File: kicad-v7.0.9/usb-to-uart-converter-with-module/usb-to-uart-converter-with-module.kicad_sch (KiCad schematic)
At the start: 10 parts, among them P1 1x10_pin_header, P2 1x10_pin_header, P3 MLW06A, Q1 MMBT2222, Q2 MMBT2222

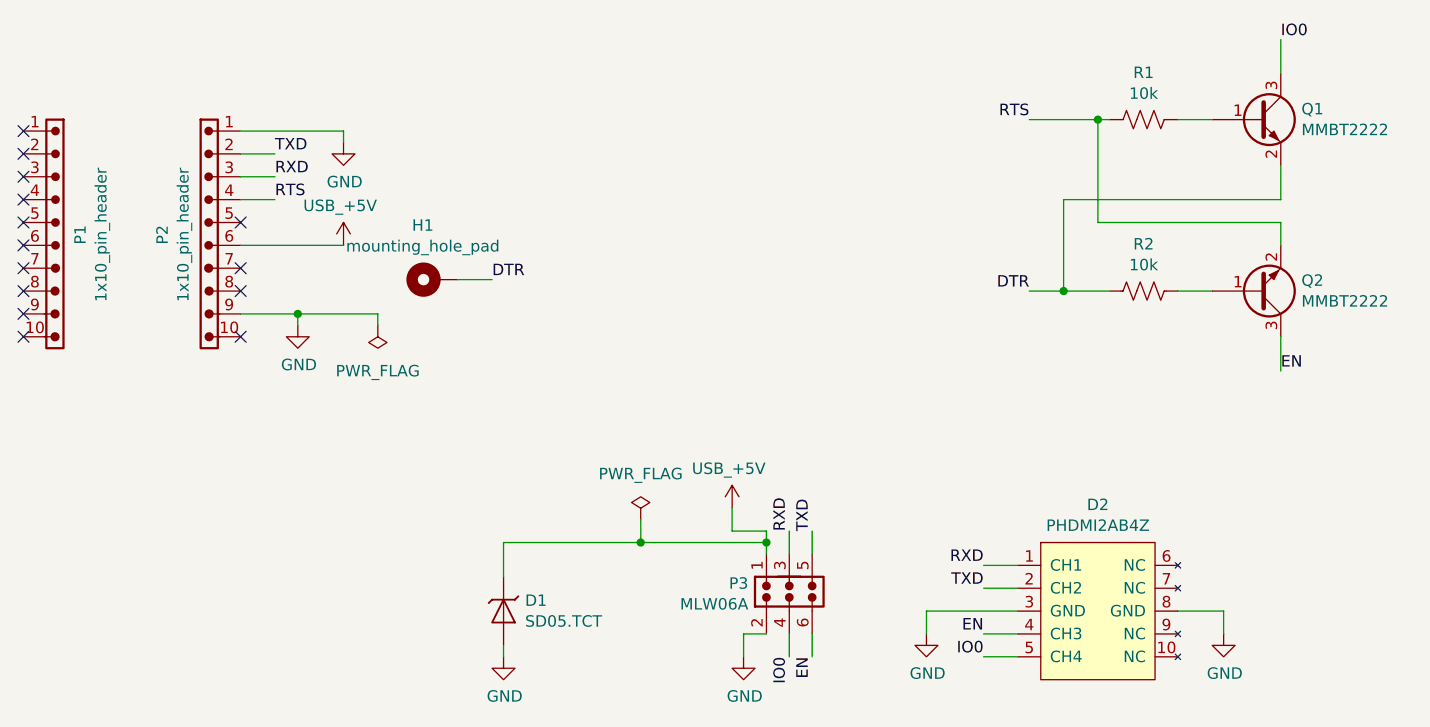
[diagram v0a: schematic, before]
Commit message: USB to UART converter. Change library. Small changes in schematic a PCB.
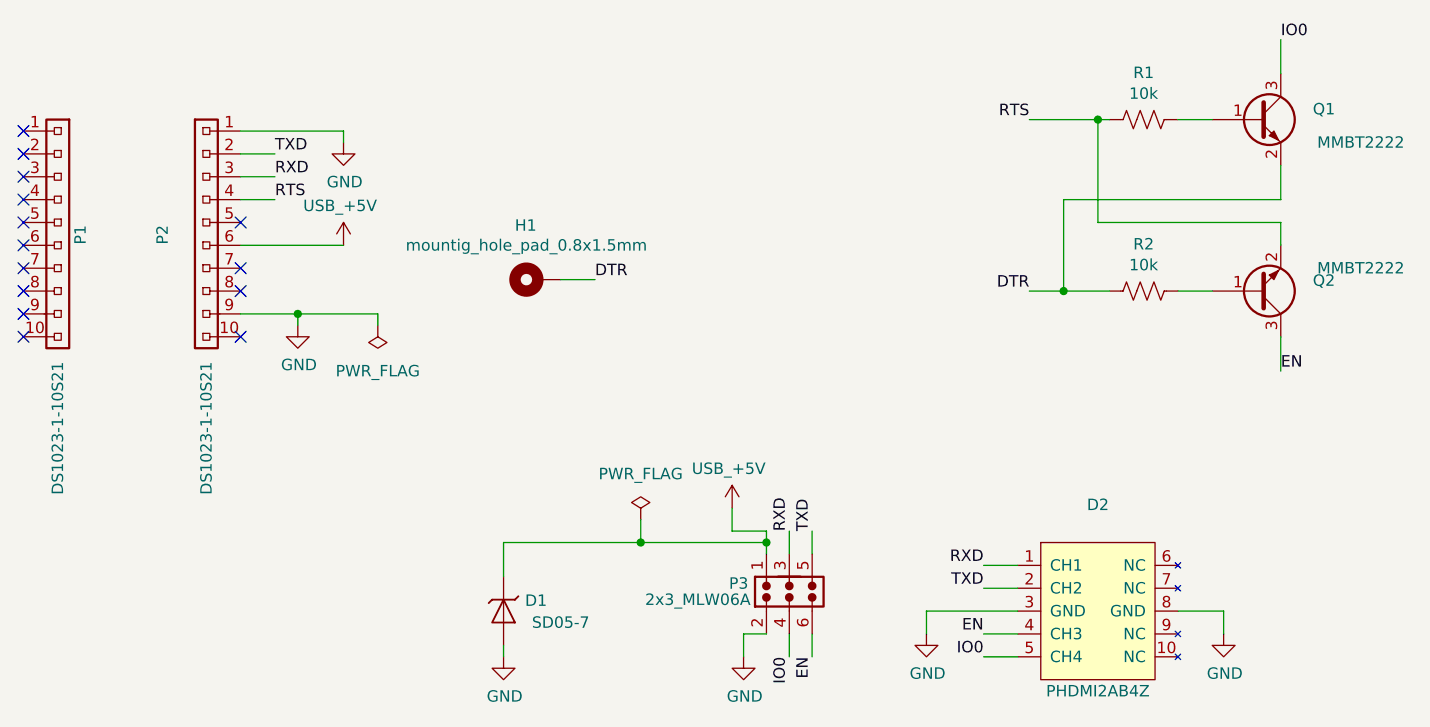
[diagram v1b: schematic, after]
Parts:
- D1: value SD05.TCT -> SD05-7; footprint diode_smd_rl:sod_323 -> package_sod_rl:sod_323; symbol diode_rl:undir_transil -> transil_diode_smd_rl:SD05-7
- D2: symbol diode_rl:PUSB3AB4 -> transil_diode_smd_rl:PHDMI2AB4Z
- H1: value mounting_hole_pad -> mountig_hole_pad_0.8x1.5mm; symbol hole_rl:mounting_hole_pad -> hole_rl:mounting_hole_pad_0.8x1.5mm; now left out of the parts list
- P1, P2: value 1x10_pin_header -> DS1023-1-10S21; footprint connector_rl:1x10_pin_header -> connector_tht_pinsocket_2.54mm_rl:1x10_pinsocket_2.54mm_vertical_8.4mm; symbol connector_rl:1x10_pin_header -> connector_tht_pin_socket_2.54mm_rl:DS1023-1-10S21
- P3: value MLW06A -> 2x3_MLW06A; footprint connector_rl:2x3_pin_header_MLW06A -> connector_idc_rl:2x3_MLW06A; symbol connector_rl:2x3_pins_header -> connector_idc_rl:2x3_MLW06A
- Q1, Q2: symbol bipolar_transistor_rl:NPN_BEC -> bipolar_transistor_smd_rl:MMBT2222
- R1, R2: symbol passive_component_rl:resistor_us -> resistor_smd_rl:r_0805_us
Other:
- moved on the sheet: H1

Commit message: Change of components from edited library. Adding of schematic in PDF.
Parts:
- H1: symbol hole_rl:mounting_hole_pad_0.8x1.5mm -> mounting_hole_pad_rl:mounting_hole_pad_0.8x1.5mm
- P1, P2: footprint connector_tht_pinsocket_2.54mm_rl:1x10_pinsocket_2.54mm_vertical_8.4mm -> connector_tht_pinsocket_2.54mm_rl:1x10_pinsocket_2.54mm_vertical_8.5mm
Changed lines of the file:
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@@
       (effects (font (size 1.27 1.27)))
     )
-    (property "Footprint" "connector_tht_pinsocket_2.54mm_rl:1x10_pinsocket_2.54mm_vertical_8.4mm" (at 110.49 69.85 0)
+    (property "Footprint" "connector_tht_pinsocket_2.54mm_rl:1x10_pinsocket_2.54mm_vertical_8.5mm" (at 110.49 69.85 0)
       (effects (font (size 1.27 1.27)) hide)
     )
@@
       (effects (font (size 1.27 1.27)))
     )
-    (property "Footprint" "connector_tht_pinsocket_2.54mm_rl:1x10_pinsocket_2.54mm_vertical_8.4mm" (at 109.22 69.85 0)
+    (property "Footprint" "connector_tht_pinsocket_2.54mm_rl:1x10_pinsocket_2.54mm_vertical_8.5mm" (at 109.22 69.85 0)
       (effects (font (size 1.27 1.27)) hide)
     )
@@
     )
   )
-  (symbol (lib_id "hole_rl:mounting_hole_pad_0.8x1.5mm") (at 153.67 74.93 90) (unit 1)
+  (symbol (lib_id "mounting_hole_pad_rl:mounting_hole_pad_0.8x1.5mm") (at 153.67 74.93 90) (unit 1)
     (in_bom no) (on_board yes) (dnp no)
     (property "Reference" "H1" (at 153.5938 68.9102 90)
@@
   (symbol (lib_id "bipolar_transistor_smd_rl:MMBT2222") (at 236.22 76.2 0) (mirror x) (unit 1)
     (in_bom yes) (on_board yes) (dnp no)
-    (property "Reference" "Q2" (at 241.046 75.0316 0)
+    (property "Reference" "Q2" (at 238.76 73.66 0)
       (effects (font (size 1.27 1.27)) (justify left))
     )
-    (property "Value" "MMBT2222" (at 246.38 73.66 0)
+    (property "Value" "MMBT2222" (at 243.84 78.74 0)
       (effects (font (size 1.27 1.27)))
     )
@@
   (symbol (lib_id "bipolar_transistor_smd_rl:MMBT2222") (at 236.22 57.15 0) (unit 1)
     (in_bom yes) (on_board yes) (dnp no)
-    (property "Reference" "Q1" (at 241.046 55.9816 0)
+    (property "Reference" "Q1" (at 240.03 54.61 0)
       (effects (font (size 1.27 1.27)) (justify left))
     )
-    (property "Value" "MMBT2222" (at 246.38 59.69 0)
-      (effects (font (size 1.27 1.27)))
-    )
+    (property "Value" "MMBT2222" (at 243.84 59.69 0)
+      (effects (font (size 1.27 1.27)))
+    )

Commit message: Change components form library. Adding of BOM.
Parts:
- P1, P2: footprint connector_tht_pinsocket_2.54mm_rl:1x10_pinsocket_2.54mm_vertical_8.5mm -> connector_pin_socket_2.54mm_tht_rl:1x10_pin_socket_2.54mm_vertical_8.5mm; symbol connector_tht_pin_socket_2.54mm_rl:DS1023-1-10S21 -> connector_pin_socket_2.54mm_tht_rl:DS1023-1-10S21
- P3: footprint connector_idc_rl:2x3_MLW06A -> connector_idc_tht_rl:2x3_MLW06A; symbol connector_idc_rl:2x3_MLW06A -> connector_idc_tht_rl:2x3_MLW06A
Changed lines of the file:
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@@
     (effects (font (size 1.27 1.27)) (justify left bottom))
   )
-  (symbol (lib_id "connector_tht_pin_socket_2.54mm_rl:DS1023-1-10S21") (at 118.11 69.85 90) (mirror x) (unit 1)
+  (symbol (lib_id "connector_pin_socket_2.54mm_tht_rl:DS1023-1-10S21") (at 118.11 69.85 90) (mirror x) (unit 1)
     (in_bom yes) (on_board yes) (dnp no)
     (property "Reference" "P2" (at 113.2332 69.9516 0)
@@
       (effects (font (size 1.27 1.27)))
     )
-    (property "Footprint" "connector_tht_pinsocket_2.54mm_rl:1x10_pinsocket_2.54mm_vertical_8.5mm" (at 110.49 69.85 0)
+    (property "Footprint" "connector_pin_socket_2.54mm_tht_rl:1x10_pin_socket_2.54mm_vertical_8.5mm" (at 110.49 69.85 0)
       (effects (font (size 1.27 1.27)) hide)
     )
@@
     )
   )
-  (symbol (lib_id "connector_tht_pin_socket_2.54mm_rl:DS1023-1-10S21") (at 101.6 69.85 270) (unit 1)
+  (symbol (lib_id "connector_pin_socket_2.54mm_tht_rl:DS1023-1-10S21") (at 101.6 69.85 270) (unit 1)
     (in_bom yes) (on_board yes) (dnp no)
     (property "Reference" "P1" (at 104.1146 69.9516 0)
@@
       (effects (font (size 1.27 1.27)))
     )
-    (property "Footprint" "connector_tht_pinsocket_2.54mm_rl:1x10_pinsocket_2.54mm_vertical_8.5mm" (at 109.22 69.85 0)
+    (property "Footprint" "connector_pin_socket_2.54mm_tht_rl:1x10_pin_socket_2.54mm_vertical_8.5mm" (at 109.22 69.85 0)
       (effects (font (size 1.27 1.27)) hide)
     )
@@
     )
   )
-  (symbol (lib_id "connector_idc_rl:2x3_MLW06A") (at 182.88 109.22 0) (mirror x) (unit 1)
+  (symbol (lib_id "connector_idc_tht_rl:2x3_MLW06A") (at 182.88 109.22 0) (mirror x) (unit 1)
     (in_bom yes) (on_board yes) (dnp no)
     (property "Reference" "P3" (at 178.3334 108.6866 0)
@@
       (effects (font (size 1.27 1.27)))
     )
-    (property "Footprint" "connector_idc_rl:2x3_MLW06A" (at 182.88 125.73 0)
+    (property "Footprint" "connector_idc_tht_rl:2x3_MLW06A" (at 182.88 125.73 0)
       (effects (font (size 1.27 1.27)) hide)
     )
